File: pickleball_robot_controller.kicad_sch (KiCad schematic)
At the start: 0 parts

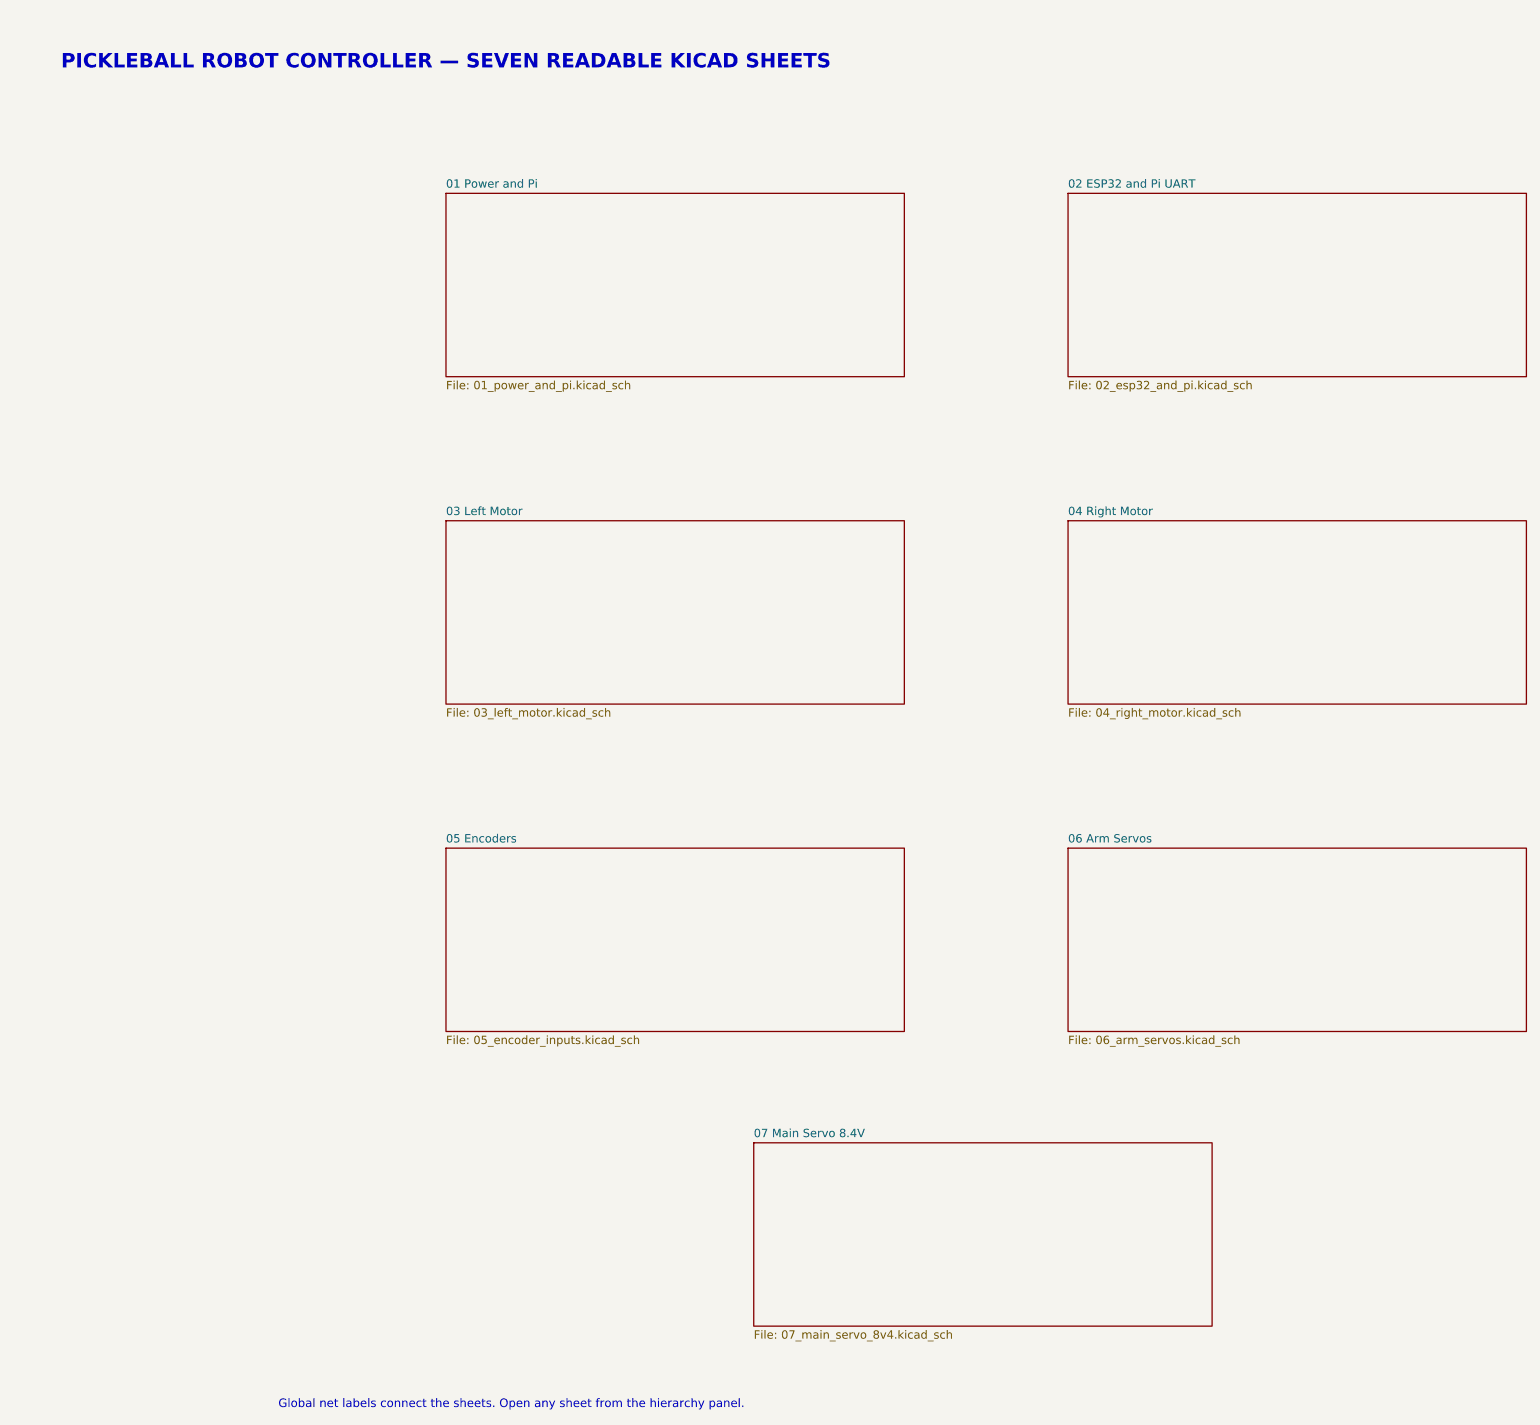
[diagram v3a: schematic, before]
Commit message: Add whole-system battery cutoff and hardened servo interfaces
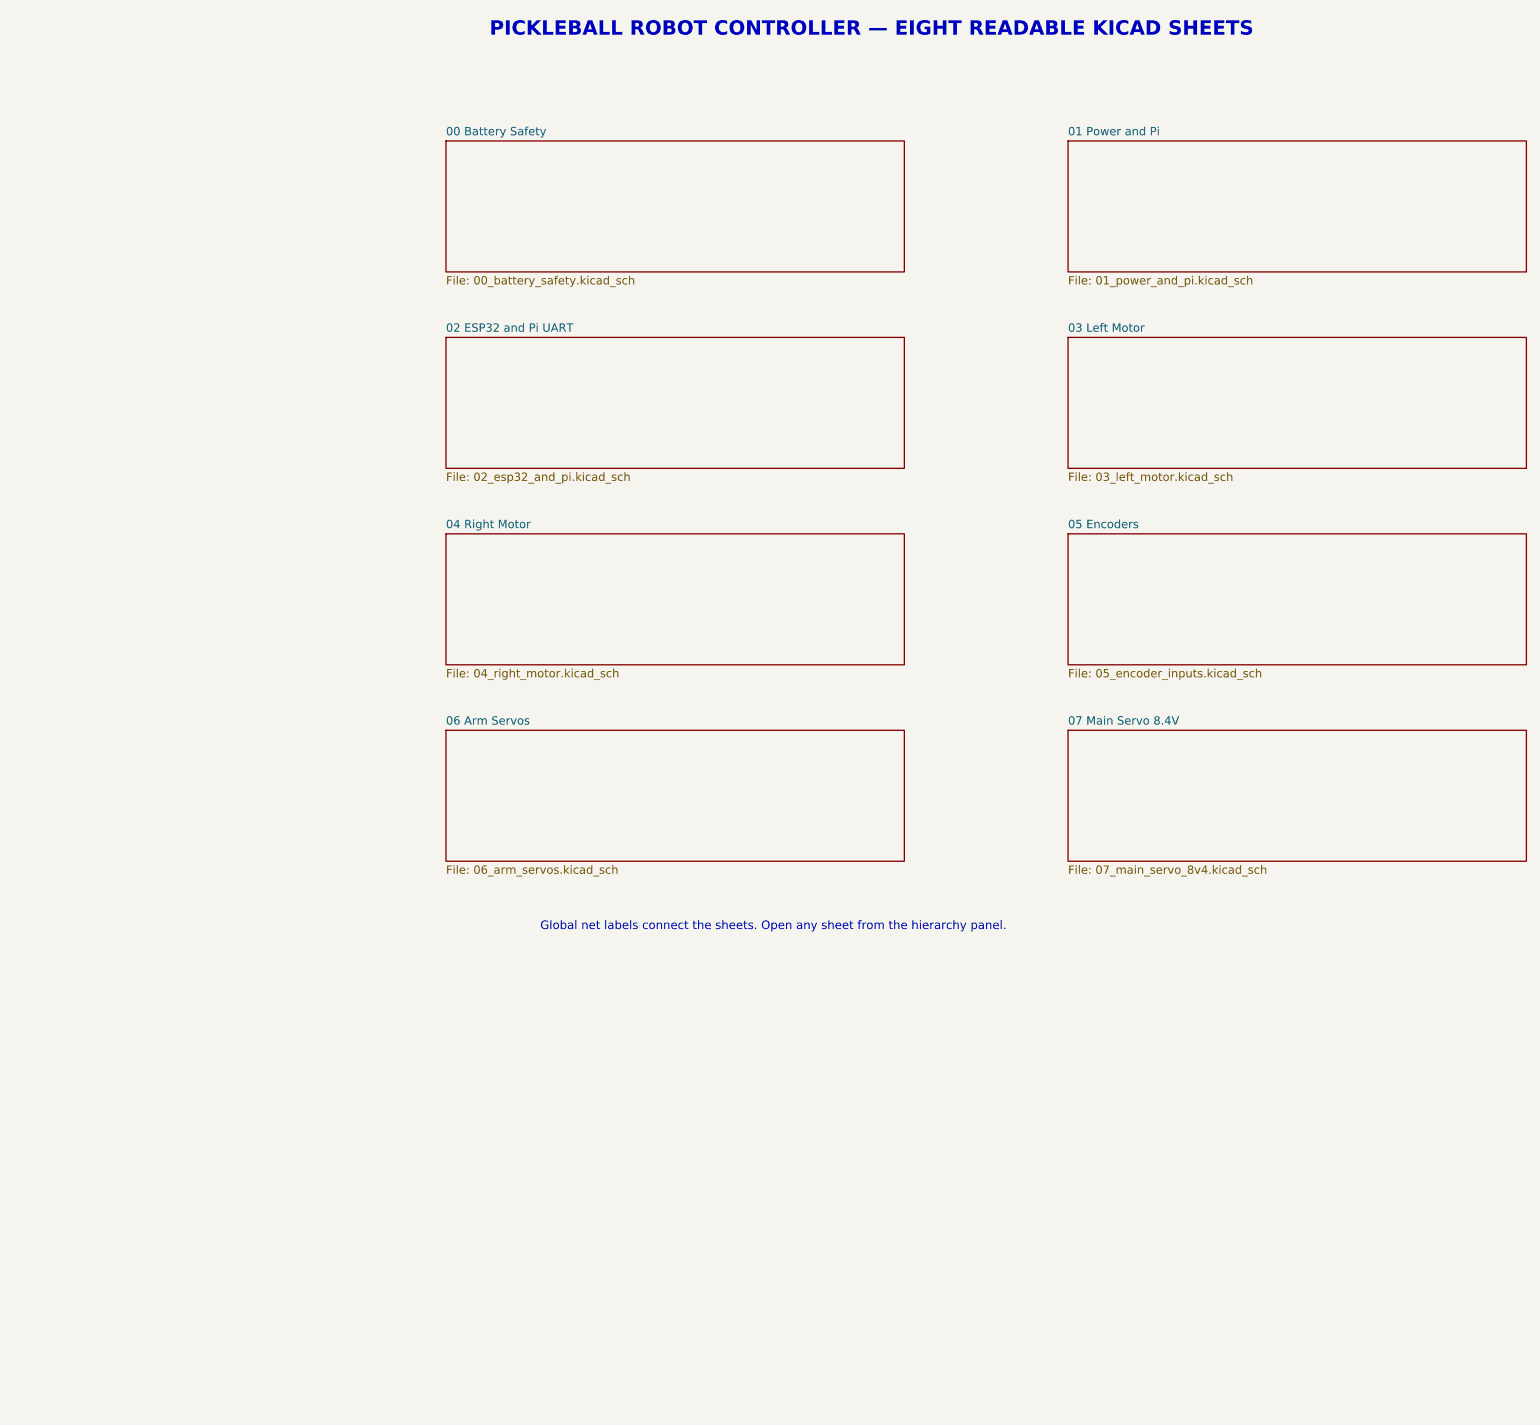
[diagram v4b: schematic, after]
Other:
- added sheet 00 Battery Safety (00_battery_safety.kicad_sch)
- note added: "PICKLEBALL ROBOT CONTROLLER — EIGHT READABLE KICAD SHEETS"
- note removed: "PICKLEBALL ROBOT CONTROLLER — SEVEN READABLE KICAD SHEETS"
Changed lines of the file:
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@@
 		(company "Harrison")
 	)
-	(text "PICKLEBALL ROBOT CONTROLLER — SEVEN READABLE KICAD SHEETS"
-		(exclude_from_sim no)
-		(at 25 20 0.0000)
+	(text "PICKLEBALL ROBOT CONTROLLER — EIGHT READABLE KICAD SHEETS"
+		(exclude_from_sim no)
+		(at 90 15 0.0000)
 		(effects
 			(font
@@
 	(text "Global net labels connect the sheets. Open any sheet from the hierarchy panel."
 		(exclude_from_sim no)
-		(at 35 225 0.0000)
+		(at 75 152 0.0000)
 		(effects
 			(font
@@
 	)
 	(sheet
-		(at 25 40)
-		(size 70 28)
+		(at 25 32)
+		(size 70 20)
+		(exclude_from_sim no)
+		(in_bom yes)
+		(on_board yes)
+		(dnp no)
+		(fields_autoplaced yes)
+		(stroke
+			(width 0.1524)
+			(type solid)
+		)
+		(fill
+			(color 0 0 0 0.0000)
+		)
+		(property "Sheetname" "00 Battery Safety"
+			(at 25 31.2884 0)
+			(effects
+				(font
+					(size 1.27 1.27)
+				)
+				(justify left bottom)
+			)
+		)
+		(property "Sheetfile" "00_battery_safety.kicad_sch"
+			(at 25 52.5846 0)
+			(effects
+				(font
+					(size 1.27 1.27)
+				)
+				(justify left top)
+			)
+		)
+		(instances
+			(project "pickleball_robot_controller"
+				(path "/235198df-6ea8-4122-bc77-bab9aaa0aa2d"
+					(page "2")
+				)
+			)
+		)
+	)
+	(sheet
+		(at 120 32)
+		(size 70 20)
 		(exclude_from_sim no)
 		(in_bom yes)
@@
 		)
 		(property "Sheetname" "01 Power and Pi"
-			(at 25 39.2884 0)
+			(at 120 31.2884 0)
 			(effects
 				(font
@@
 		)
 		(property "Sheetfile" "01_power_and_pi.kicad_sch"
-			(at 25 68.5846 0)
-			(effects
-				(font
-					(size 1.27 1.27)
-				)
-				(justify left top)
-			)
-		)
-		(instances
-			(project "pickleball_robot_controller"
-				(path "/35c0251d-1373-4862-b811-49b8a8b23e09"
-					(page "2")
-				)
-			)
-		)
-	)
-	(sheet
-		(at 120 40)
-		(size 70 28)
+			(at 120 52.5846 0)
+			(effects
+				(font
+					(size 1.27 1.27)
+				)
+				(justify left top)
+			)
+		)
+		(instances
+			(project "pickleball_robot_controller"
+				(path "/235198df-6ea8-4122-bc77-bab9aaa0aa2d"
+					(page "3")
+				)
+			)
+		)
+	)
+	(sheet
+		(at 25 62)
+		(size 70 20)
 		(exclude_from_sim no)
 		(in_bom yes)
@@
 		)
 		(property "Sheetname" "02 ESP32 and Pi UART"
-			(at 120 39.2884 0)
+			(at 25 61.2884 0)
 			(effects
 				(font
@@
 		)
 		(property "Sheetfile" "02_esp32_and_pi.kicad_sch"
-			(at 120 68.5846 0)
-			(effects
-				(font
-					(size 1.27 1.27)
-				)
-				(justify left top)
-			)
-		)
-		(instances
-			(project "pickleball_robot_controller"
-				(path "/35c0251d-1373-4862-b811-49b8a8b23e09"
-					(page "3")
-				)
-			)
-		)
-	)
-	(sheet
-		(at 25 90)
-		(size 70 28)
+			(at 25 82.5846 0)
+			(effects
+				(font
+					(size 1.27 1.27)
+				)
+				(justify left top)
+			)
+		)
+		(instances
+			(project "pickleball_robot_controller"
+				(path "/235198df-6ea8-4122-bc77-bab9aaa0aa2d"
+					(page "4")
+				)
+			)
+		)
+	)
+	(sheet
+		(at 120 62)
+		(size 70 20)
 		(exclude_from_sim no)
 		(in_bom yes)
@@
 		)
 		(property "Sheetname" "03 Left Motor"
-			(at 25 89.2884 0)
+			(at 120 61.2884 0)
 			(effects
 				(font
@@
 		)
 		(property "Sheetfile" "03_left_motor.kicad_sch"
-			(at 25 118.5846 0)
-			(effects
-				(font
-					(size 1.27 1.27)
-				)
-				(justify left top)
-			)
-		)
-		(instances
-			(project "pickleball_robot_controller"
-				(path "/35c0251d-1373-4862-b811-49b8a8b23e09"
-					(page "4")
-				)
-			)
-		)
-	)
-	(sheet
-		(at 120 90)
-		(size 70 28)
+			(at 120 82.5846 0)
+			(effects
+				(font
+					(size 1.27 1.27)
+				)
+				(justify left top)
+			)
+		)
+		(instances
+			(project "pickleball_robot_controller"
+				(path "/235198df-6ea8-4122-bc77-bab9aaa0aa2d"
+					(page "5")
+				)
+			)
+		)
+	)
+	(sheet
+		(at 25 92)
+		(size 70 20)
 		(exclude_from_sim no)
 		(in_bom yes)
@@
 		)
 		(property "Sheetname" "04 Right Motor"
-			(at 120 89.2884 0)
+			(at 25 91.2884 0)
 			(effects
 				(font
@@
 		)
 		(property "Sheetfile" "04_right_motor.kicad_sch"
-			(at 120 118.5846 0)
-			(effects
-				(font
-					(size 1.27 1.27)
-				)
-				(justify left top)
-			)
-		)
-		(instances
-			(project "pickleball_robot_controller"
-				(path "/35c0251d-1373-4862-b811-49b8a8b23e09"
-					(page "5")
-				)
-			)
-		)
-	)
-	(sheet
-		(at 25 140)
-		(size 70 28)
+			(at 25 112.5846 0)
+			(effects
+				(font
+					(size 1.27 1.27)
+				)
+				(justify left top)
+			)
+		)
+		(instances
+			(project "pickleball_robot_controller"
+				(path "/235198df-6ea8-4122-bc77-bab9aaa0aa2d"
+					(page "6")
+				)
+			)
+		)
+	)
+	(sheet
+		(at 120 92)
+		(size 70 20)
 		(exclude_from_sim no)
 		(in_bom yes)
@@
 		)
 		(property "Sheetname" "05 Encoders"
-			(at 25 139.2884 0)
+			(at 120 91.2884 0)
 			(effects
 				(font
@@
 		)
 		(property "Sheetfile" "05_encoder_inputs.kicad_sch"
-			(at 25 168.5846 0)
-			(effects
-				(font
-					(size 1.27 1.27)
-				)
-				(justify left top)
-			)
-		)
-		(instances
-			(project "pickleball_robot_controller"
-				(path "/35c0251d-1373-4862-b811-49b8a8b23e09"
-					(page "6")
-				)
-			)
-		)
-	)
-	(sheet
-		(at 120 140)
-		(size 70 28)
+			(at 120 112.5846 0)
+			(effects
+				(font
+					(size 1.27 1.27)
+				)
+				(justify left top)
+			)
+		)
+		(instances
+			(project "pickleball_robot_controller"
+				(path "/235198df-6ea8-4122-bc77-bab9aaa0aa2d"
+					(page "7")
+				)
+			)
+		)
+	)
+	(sheet
+		(at 25 122)
+		(size 70 20)
 		(exclude_from_sim no)
 		(in_bom yes)
@@
 		)
 		(property "Sheetname" "06 Arm Servos"
-			(at 120 139.2884 0)
+			(at 25 121.2884 0)
 			(effects
 				(font
@@
 		)
 		(property "Sheetfile" "06_arm_servos.kicad_sch"
-			(at 120 168.5846 0)
-			(effects
-				(font
-					(size 1.27 1.27)
-				)
-				(justify left top)
-			)
-		)
-		(instances
-			(project "pickleball_robot_controller"
-				(path "/35c0251d-1373-4862-b811-49b8a8b23e09"
-					(page "7")
-				)
-			)
-		)
-	)
-	(sheet
-		(at 72 185)
-		(size 70 28)
+			(at 25 142.5846 0)
+			(effects
+				(font
+					(size 1.27 1.27)
+				)
+				(justify left top)
+			)
+		)
+		(instances
+			(project "pickleball_robot_controller"
+				(path "/235198df-6ea8-4122-bc77-bab9aaa0aa2d"
+					(page "8")
+				)
+			)
+		)
+	)
+	(sheet
+		(at 120 122)
+		(size 70 20)
 		(exclude_from_sim no)
 		(in_bom yes)
@@
 		)
 		(property "Sheetname" "07 Main Servo 8.4V"
-			(at 72 184.2884 0)
+			(at 120 121.2884 0)
 			(effects
 				(font
@@
 		)
 		(property "Sheetfile" "07_main_servo_8v4.kicad_sch"
-			(at 72 213.5846 0)
-			(effects
-				(font
-					(size 1.27 1.27)
-				)
-				(justify left top)
-			)
-		)
-		(instances
-			(project "pickleball_robot_controller"
-				(path "/35c0251d-1373-4862-b811-49b8a8b23e09"
-					(page "8")
-				)
-			)
+			(at 120 142.5846 0)
+			(effects
+				(font
+					(size 1.27 1.27)
+				)
+				(justify left top)
+			)
+		)
+		(instances
+			(project "pickleball_robot_controller"
+				(path "/235198df-6ea8-4122-bc77-bab9aaa0aa2d"
+					(page "9")
+				)
+			)
